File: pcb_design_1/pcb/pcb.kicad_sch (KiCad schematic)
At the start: 0 parts

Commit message: add modify implement
add modify implement
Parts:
- added J1: Conn_01x06_Pin, symbol Connector:Conn_01x06_Pin
- added J2: Screw_Terminal_01x02, symbol Connector:Screw_Terminal_01x02
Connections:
- new net 3.3V: J1.5 (Pin_5), J1.6 (Pin_6)
- new net 5V: J1.1 (Pin_1), J1.2 (Pin_2)
- new net BAT_in: J2.1 (Pin_1)
- new net GND: J1.3 (Pin_3), J1.4 (Pin_4), J2.2 (Pin_2)
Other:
- added sheet ESP32 (ESP32.kicad_sch)
- added sheet PCF8574 (PCF8574.kicad_sch)
- added sheet Power_Supply (Power_Supply.kicad_sch)
- added sheet TB6612 (TB6612.kicad_sch)

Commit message: Add TOF sensor sheet and move I2C resistors
- Created new Sensors_TOF schematic sheet for Time-of-Flight sensor with I2C interface
- Moved I2C pull-up resistors (R8, R9, 2k ohm) from PCF8574 to ESP32 sheet
- Added hierarchical labels (SDA, SCL, 3.3v) to ESP32 sheet for I2C connectivity
- Added TOF sensor connector (J7) with 6-pin socket connection
- Updated project designators in pcb.kicad_pro
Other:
- added sheet Sensors_TOF (Sensors_TOF.kicad_sch)
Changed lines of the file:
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@@
+	)
+	(sheet
+		(at 219.71 102.87)
+		(size 34.29 27.94)
+		(exclude_from_sim no)
+		(in_bom yes)
+		(on_board yes)
+		(dnp no)
+		(fields_autoplaced yes)
+		(stroke
+			(width 0.1524)
+			(type solid)
+		)
+		(fill
+			(color 0 0 0 0)
+		)
+		(property "Sheetname" "Sensors_TOF"
+			(at 219.71 102.1584 0)
+			(show_name no)
+			(do_not_autoplace no)
+			(effects
+				(font
+					(size 1.27 1.27)
+				)
+				(justify left bottom)
+			)
+		)
+		(property "Sheetfile" "Sensors_TOF.kicad_sch"
+			(at 219.71 131.3946 0)
+			(show_name no)
+			(do_not_autoplace no)
+			(effects
+				(font
+					(size 1.27 1.27)
+				)
+				(justify left top)
+			)
+		)
+		(instances
+			(project "pcb"
+				(path "/641f7b51-eb90-47ac-8b04-a4718aaaca74"
+					(page "8")
+				)
+			)
+		)
 	)
 	(sheet

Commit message: Add OLED Display and power switch, rename battery input
Added new OLED Display schematic sheet with I2C connector (J14) and pinout. Integrated OLED display connections (VCC, GND, SDA, SCL) into main PCB. Added power switch (SW1) between battery input and power supply. Renamed battery input signal from 'battery_in' to 'battery_in_1' throughout 5V input and power supply sheets. Updated component designators and repositioned schematic sheets for improved layout organization.
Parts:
- added SW1: SW_SPST, symbol Switch:SW_SPST
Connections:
- net BAT_in: now also SW1.1 (A)
- new net BAT_in_1: SW1.2 (B)
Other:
- added sheet OLED_Display (OLED_Display.kicad_sch)
- sheet Power_Supply ports: added Bat_in_1; removed Bat_in
- sheet Sensors_TOF ports: added GND, GPIO_1, GPIO_2, GPIO_3, GPIO_4, GPIO_5, SCL, SDA, VCC, Xshunt_1, Xshunt_2, Xshunt_3, Xshunt_4, Xshunt_5; removed none

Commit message: improved the designed
improved the designed
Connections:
- no-connect marks 0 -> 16
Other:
- added sheet TCA9548A (TCA9548A.kicad_sch)
- sheet OLED_Display ports: added SCL, SDA, VCC; removed none
- sheet Sensors_TOF ports: added SCL_1, SCL_2, SCL_3, SCL_4, SCL_5, SDA_1, SDA_2, SDA_3, SDA_4, SDA_5; removed SCL, SDA
- moved on the sheet: J1, J2, SW1

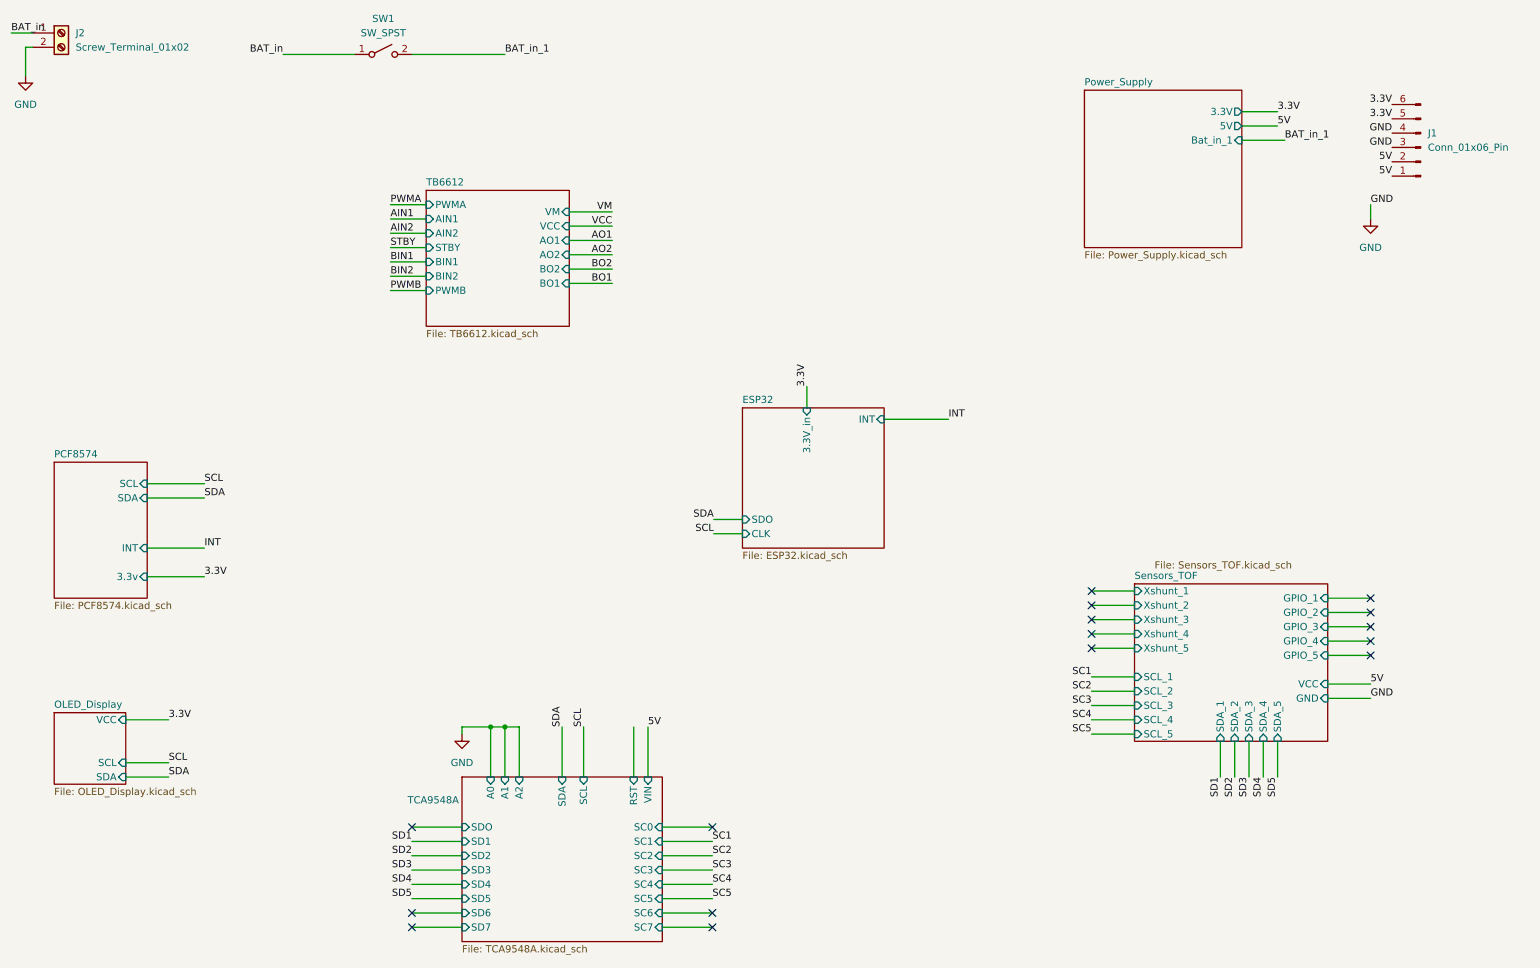
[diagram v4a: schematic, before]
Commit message: Update KiCad sheet wiring
Adjust schematic hierarchy and net connections across the PCB project, including ESP32, TCA9548A, OLED, sensors, switches, and indication sheets. Adds R1 and updates sheet pin labels, wire placement, and project designator metadata to match the revised net naming and connectivity.
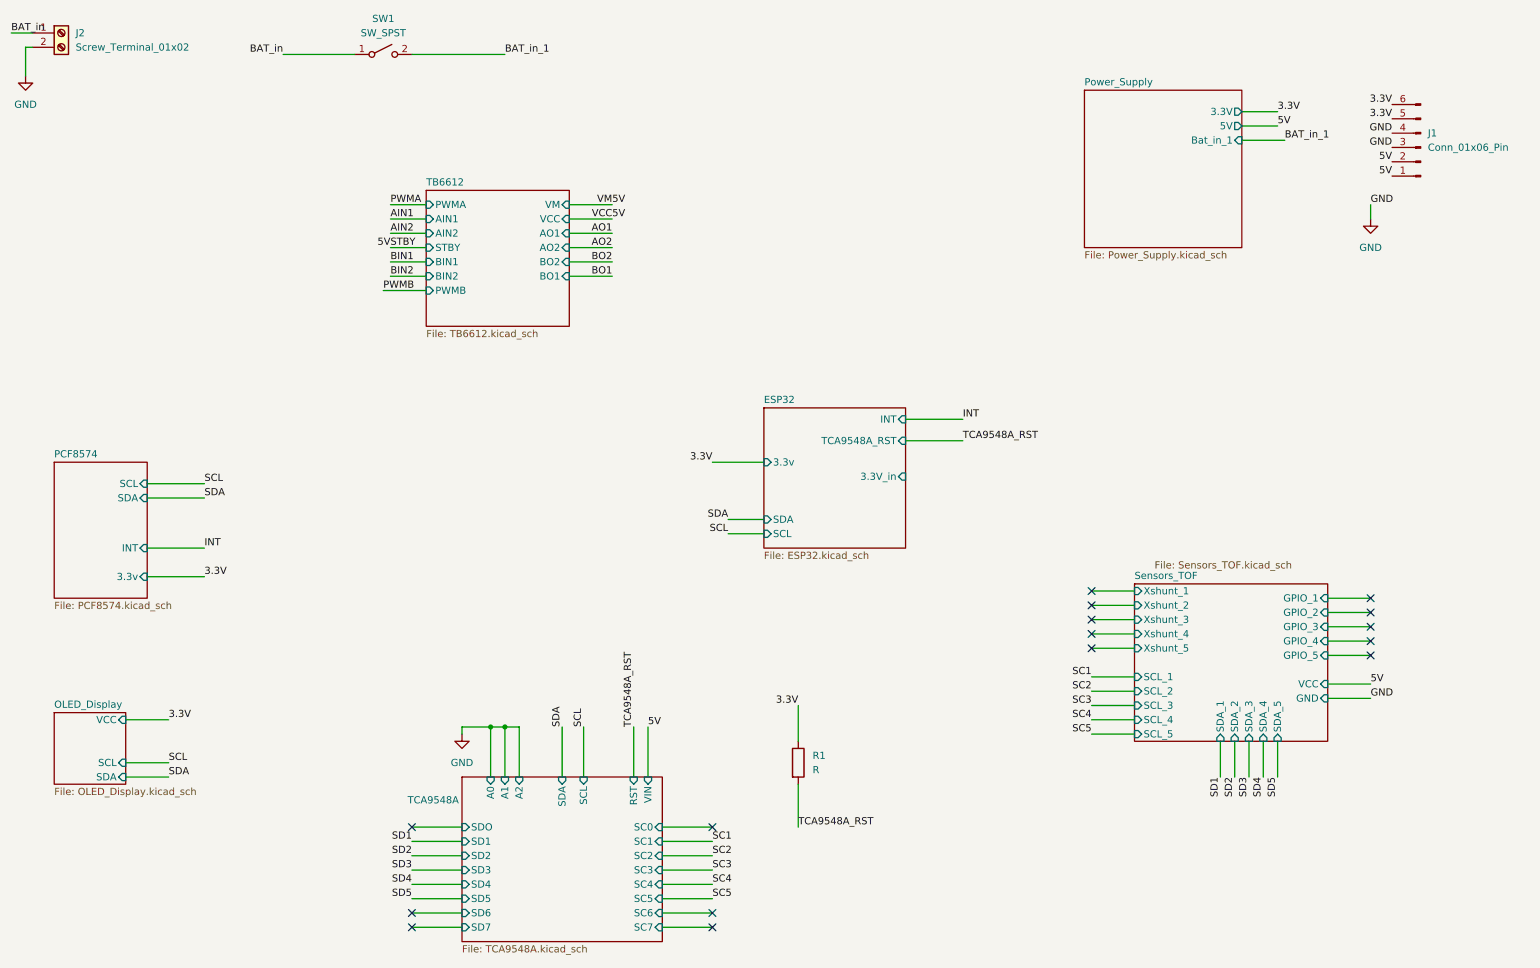
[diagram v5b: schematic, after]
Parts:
- added R1: R, symbol Device:R
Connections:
- net 3.3V: now also R1.1
- new net TCA9548A_RST: R1.2
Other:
- sheet ESP32 ports: added 3.3v, SCL, SDA, TCA9548A_RST; removed CLK, SDO
